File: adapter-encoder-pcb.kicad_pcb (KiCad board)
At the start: 2 copper layers, 12 x 12 mm, 21 parts, among them IC1 THVD2410VDRCR, M1 THRU_HOLE_PAD, M2 THRU_HOLE_PAD, U1 TLE5009E1000FUMA1, U2 STM32L011F4Ux, U3 DF52-4S-0.8H(21), U4 SPX3819M5-L-3-3

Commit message: mostly routed updated board
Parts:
- added C12: 4.7uF, adapter-encoder:C_0603_1608Metric, F.Cu at (139.5, 111.0)
- added C13: 100nF, adapter-encoder:C_0402_1005Metric, F.Cu at (138.5, 111.1)
- added C14: 100nF, adapter-encoder:C_0402_1005Metric, B.Cu at (141.1, 107.9)
- added C15: 4.7uF, adapter-encoder:C_0603_1608Metric, B.Cu at (142.4, 106.7)
- added C16: 100nF, adapter-encoder:C_0402_1005Metric, B.Cu at (148.7, 107.2)
- added C17: 4.7uF, adapter-encoder:C_0603_1608Metric, B.Cu at (147.6, 107.0)
- added C18: 100nF, adapter-encoder:C_0402_1005Metric, F.Cu at (146.7, 113.8)
- added D1: LED, adapter-encoder:LED_0603_1608Metric, F.Cu at (140.4, 115.9)
- added R1: Resistor, adapter-encoder:R_0402_1005Metric, B.Cu at (141.7, 116.1)
- added U5: C2901617, adapter-encoder:ECS-1633-480-BN-TR, F.Cu at (140.4, 113.2)
- added U6: DF52-4S-0.8H(21), adapter-encoder:DF52-4S-0.8H(21), F.Cu at (144.9, 106.6)
- added U7: SPX3819M5-L-3-3, adapter-encoder:SOT-23-5, B.Cu at (145.0, 106.7)
- U2: value STM32L011F4Ux -> STM32G031G6U6; footprint adapter-encoder:ST_UFQFPN-20_3x3mm_P0.5mm -> adapter-encoder:UFQFPN28
- moved C8 4.84 mm to (145.8, 113.8), turned to 90 degrees
- moved C1 4.29 mm to (143.9, 113.8), turned to 0 degrees
- moved C5 4.14 mm to (143.5, 112.7), turned to 0 degrees
- moved R3 3.98 mm to (150.1, 110.7), turned to 90 degrees
- moved R4 3.48 mm to (149.3, 111.5), turned to 90 degrees
- moved M1 3.02 mm to (139.4, 108.7), turned to 90 degrees
- moved C7 2.73 mm to (148.5, 108.6), turned to 0 degrees
- moved C11 2.68 mm to (143.7, 115.2), turned to 90 degrees
- moved C3 2.65 mm to (142.0, 112.9)
- moved R2 2.63 mm to (149.3, 110.1), turned to 90 degrees
- moved U3 2.50 mm to (144.9, 116.6)
- moved C6 2.43 mm to (146.3, 108.6), turned to 180 degrees
- moved C4 2.11 mm to (141.1, 109.3), turned to 90 degrees
- moved IC1 1.61 mm to (147.1, 110.9), turned to 0 degrees
- moved M2 1.41 mm to (140.9, 106.7), turned to 90 degrees
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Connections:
- C1 pad 1: /3v3 -> +3V3
- C3 pad 1: /3v3 -> +3V3
- C5 pad 1: Net-(U2-NRST) -> Net-(U2-PF2-NRST)
- U1 pad 6: /3v3 -> +3V3
- U2 pad 1: unconnected-(U2-PC14-Pad1) -> Net-(U2-PC14-OSC32_IN)
- U2 pad 10: /UART1_DE -> unconnected-(U2-PA4-Pad10)
- U2 pad 11: /LED_GPIO -> unconnected-(U2-PA5-Pad11)
- U2 pad 12: GND -> unconnected-(U2-PA6-Pad12)
- U2 pad 13: /3v3 -> unconnected-(U2-PA7-Pad13)
- U2 pad 14: /TX -> unconnected-(U2-PB0-Pad14)
- U2 pad 15: /RX -> unconnected-(U2-PB1-Pad15)
- U2 pad 16: /SWDIO -> unconnected-(U2-PA8-Pad16)
- U2 pad 17: /SWCLK -> /UART1_DE
- U2 pad 20: GND -> /SWCLK
- U2 pad 3: Net-(U2-NRST) -> +3V3
- U2 pad 4: /3v3 -> GND
- U2 pad 5: /V_TEMP -> Net-(U2-PF2-NRST)
- U2 pad 6: unconnected-(U2-PA1-Pad6) -> /SIN
- U2 pad 7: /SIN -> /COS
- U2 pad 8: /COS -> /TX
- U2 pad 9: unconnected-(U2-PA6-Pad9) -> /RX
- U4 pad 5: /3v3 -> +3V3
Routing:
- net /Vin: track 11.7 -> 35.8 mm, vias 1 -> 4
- net +3V3: track 1.45 -> 22.6 mm, vias 0 -> 4
- net /B-PROTECTED: track 4.36 -> 21.1 mm, vias 0 -> 2
- net /A-PROTECTED: track 4.35 -> 20.6 mm, vias 0 -> 2
- net /3v3: track 8.76 -> 0.00 mm, vias 1 -> 0
- net /LED_GPIO: track 0.00 -> 6.73 mm, vias 0 -> 2
- net /RX: track 6.75 -> 1.51 mm
- net /+5V0: track 2.01 -> 6.63 mm, vias 0 -> 1
- net /UART1_DE: track 8.89 -> 5.91 mm
- net /COS: track 10.0 -> 7.13 mm
- net /TX: track 3.99 -> 1.51 mm
- net Net-(D1-K): track 0.00 -> 1.72 mm, vias 0 -> 1
- net GND: track 1.69 -> 0.00 mm, vias 18 -> 19
- net /SIN: track 6.90 -> 5.28 mm
- net Net-(U2-PF2-NRST): track 0.00 -> 0.96 mm
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- added copper zone on In1.Cu, net GND
- added copper zone on In2.Cu, net GND
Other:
- board size 12 x 12 mm -> 14 x 14 mm
- copper layers 2 -> 4

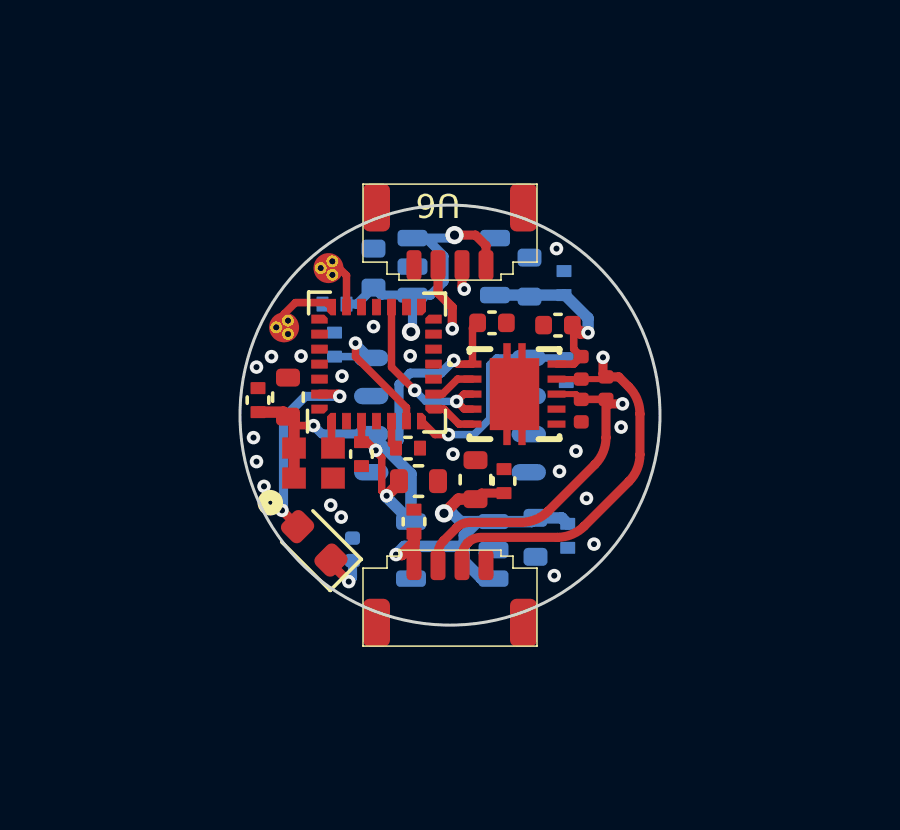
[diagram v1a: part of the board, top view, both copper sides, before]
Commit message: deleted unnecessary files, updated board outline, drc passes
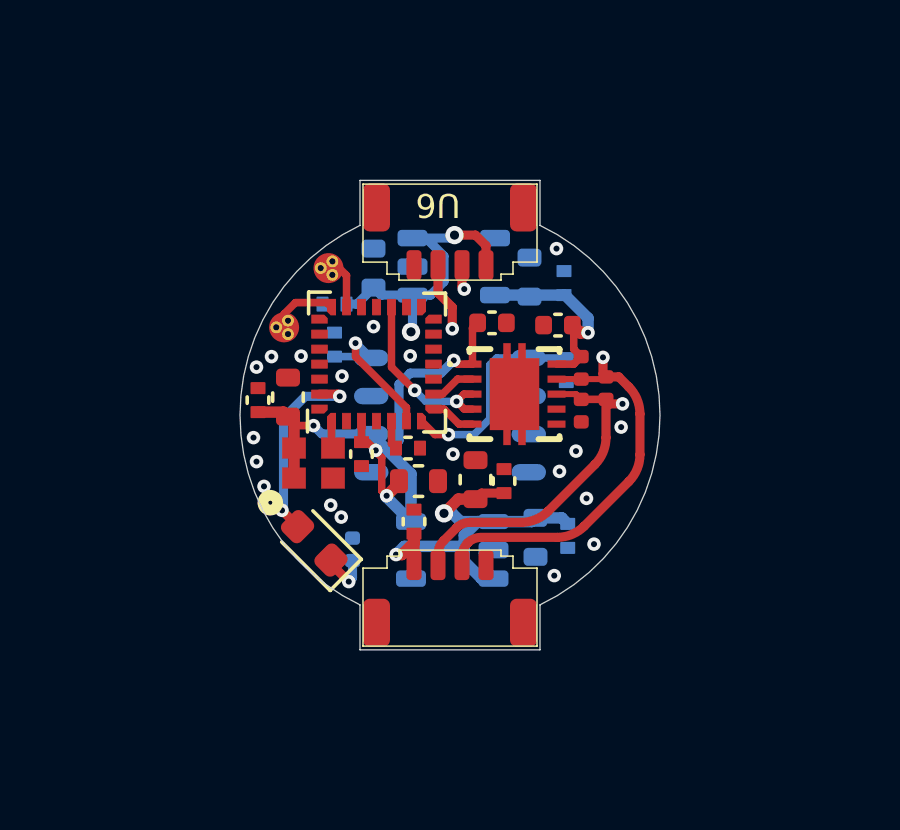
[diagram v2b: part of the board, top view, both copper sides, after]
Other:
- board size 14 x 14 mm -> 14 x 15.6 mm
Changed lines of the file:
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@@
     )
   )
-  (gr_circle (center 144.904448 111.637448) (end 151.904448 111.637448)
-    (stroke (width 0.1) (type default)) (fill none) (layer "Edge.Cuts"))
+  (gr_line (start 147.90446 117.962127) (end 147.90446 119.462127)
+    (stroke (width 0.0254) (type solid)) (layer "Edge.Cuts"))
+  (gr_line (start 141.90446 103.813017) (end 147.90446 103.813017)
+    (stroke (width 0.0254) (type solid)) (layer "Edge.Cuts"))
+  (gr_line (start 141.90446 105.313017) (end 141.90446 103.813017)
+    (stroke (width 0.0254) (type solid)) (layer "Edge.Cuts"))
+  (gr_arc (start 147.90446 105.313017) (mid 151.904458 111.637571) (end 147.90446 117.962127)
+    (stroke (width 0.0254) (type solid)) (layer "Edge.Cuts"))
+  (gr_arc (start 141.90446 117.962127) (mid 137.904458 111.637571) (end 141.90446 105.313017)
+    (stroke (width 0.0254) (type solid)) (layer "Edge.Cuts"))
+  (gr_line (start 147.90446 119.462127) (end 141.90446 119.462127)
+    (stroke (width 0.0254) (type solid)) (layer "Edge.Cuts"))
+  (gr_line (start 147.90446 103.813017) (end 147.90446 105.313017)
+    (stroke (width 0.0254) (type solid)) (layer "Edge.Cuts"))
+  (gr_line (start 141.90446 119.462127) (end 141.90446 117.962127)
+    (stroke (width 0.0254) (type solid)) (layer "Edge.Cuts"))
   (via (at 150.608848 112.037448) (size 0.45) (drill 0.2) (layers "F.Cu" "B.Cu") (net 1))
   (via (at 148.379448 116.987448) (size 0.45) (drill 0.2) (layers "F.Cu" "B.Cu") (net 1))
